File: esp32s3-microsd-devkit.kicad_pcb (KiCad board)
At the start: 4 copper layers, 53.1 x 49.5 mm, 28 parts, among them J1 Conn_01x17, J2 USB4105-GF-A, J3 Conn_01x17, U1 ESP32-S3-WROOM-1, U2 USBLC6-2P6, U3 MIC23150-SYMT-TR, X1 DM3AT-SF-PEJM5

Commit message: Ready to make v0.1
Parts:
- added D2: B0540WS-TP, Diode_SMD:D_SOD-123, F.Cu at (125.7, 91.0)
- added H1: MountingHole, MountingHole:MountingHole_2.2mm_M2_ISO7380_Pad, F.Cu at (121.0, 117.5)
- added H2: MountingHole, MountingHole:MountingHole_2.2mm_M2_ISO7380_Pad, F.Cu at (170.2, 69.2)
- added H3: MountingHole, MountingHole:MountingHole_2.2mm_M2_ISO7380_Pad, F.Cu at (170.2, 117.5)
- added TP1: TestPoint, TestPoint:TestPoint_Pad_1.5x1.5mm, F.Cu at (135.2, 107.9)
- added TP2: TestPoint, TestPoint:TestPoint_Pad_1.5x1.5mm, F.Cu at (127.7, 107.8)
- added TP3: TestPoint, TestPoint:TestPoint_Pad_1.5x1.5mm, F.Cu at (131.4, 107.8)
- moved J3 4.26 mm to (125.1, 117.5)
- moved J1 4.02 mm to (170.2, 73.0)
- renumbered BOOT1 to BOOT, RESET1 to RESET
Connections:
- J2 pad A4: +5V -> Net-(D2-A)
- J2 pad A9: +5V -> Net-(D2-A)
- J2 pad B4: +5V -> Net-(D2-A)
- J2 pad B9: +5V -> Net-(D2-A)
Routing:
- net Net-(D2-A): track 0.00 -> 41.6 mm, vias 0 -> 3
- net +3.3V: track 160.5 -> 170.2 mm
- net GPIO_35: track 17.4 -> 25.1 mm
- net +5V: track 90.1 -> 82.7 mm, vias 0 -> 3
- net GPIO_36: track 17.0 -> 23.7 mm
- net GPIO_39: track 14.6 -> 20.5 mm
- net GPIO_37: track 16.2 -> 22.1 mm
- net GPIO_45: track 19.9 -> 25.5 mm
- net GPIO_38: track 15.7 -> 21.1 mm
- net GPIO_40: track 13.7 -> 18.8 mm
- net GPIO_41: track 12.3 -> 17.1 mm
- net GPIO_21: track 29.5 -> 34.1 mm
- net GPIO_48: track 30.6 -> 35.2 mm
- net GPIO_47: track 30.0 -> 34.6 mm
- net GPIO_14: track 29.0 -> 33.6 mm
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- added copper zone on In2.Cu, net +3.3V
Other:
- board size 53.1 x 49.5 mm -> 54.4 x 53.3 mm
- board text added: "1"
- board text added: "10"
- board text added: "11"
- board text added: "12"
- board text added: "13"
- board text added: "14"
- board text added: "17"
- board text added: "18"
- board text added: "2"
- board text added: "21"
- board text added: "3"
- board text added: "3.3v"
- board text added: "35"
- board text added: "36"
- board text added: "37"
- board text added: "38"
- board text added: "39"
- board text added: "40"
- board text added: "41"
- board text added: "42"
- board text added: "45"
- board text added: "46"
- board text added: "47"
- board text added: "48"
- board text added: "5v"
- board text added: "8"
- board text added: "9"
- board text added: "ESP32S3 SD Devkit v0.1"
- board text added: "G"
- board text added: "GND"
- board text added: "RX"
- board text added: "Ride like a maniac into the light"
- board text added: "TX"

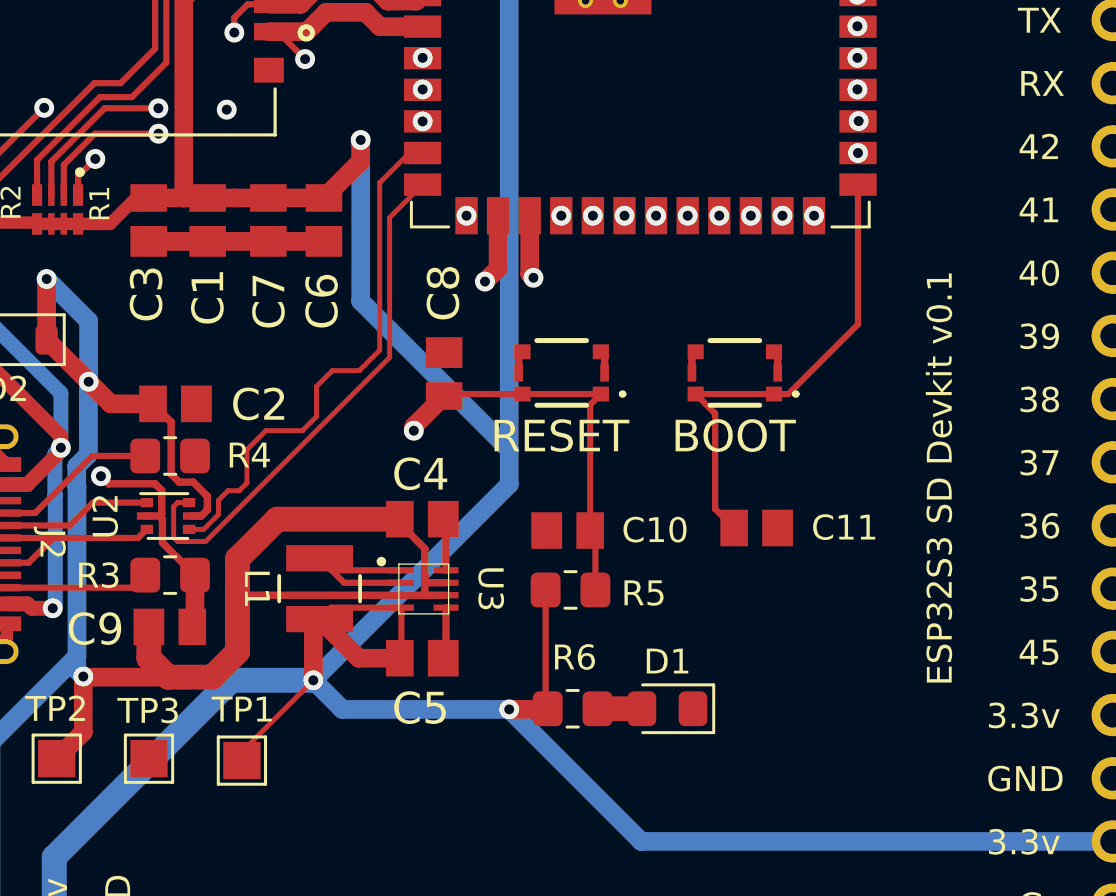
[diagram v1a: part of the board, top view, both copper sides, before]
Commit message: Fix cross-wired USB lines
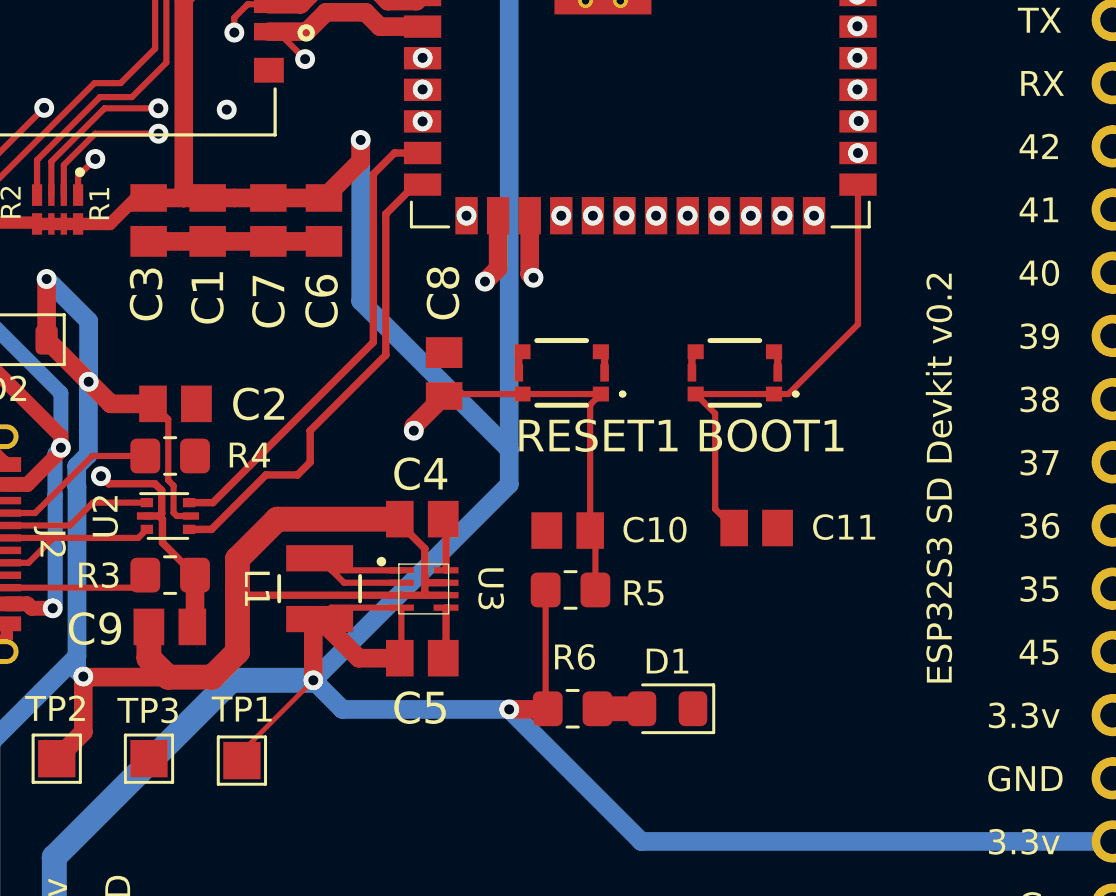
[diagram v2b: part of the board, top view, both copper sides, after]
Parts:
- added G***: LOGO, LOGO, B.Cu at (145.3, 91.8)
- renumbered BOOT to BOOT1, RESET to RESET1
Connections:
- U1 pad 13: /USB C/USB_D+ -> /USB C/USB_D-
- U1 pad 14: /USB C/USB_D- -> /USB C/USB_D+
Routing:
- net /USB C/USB_D+: track 21.4 -> 19.2 mm
- net /USB C/USB_D-: track 21.2 -> 19.2 mm
- net +5V: track 82.7 -> 82.0 mm
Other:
- board text added: "ESP32S3 SD Devkit v0.2"
- board text added: "Spidergod Industries"
- board text removed: "ESP32S3 SD Devkit v0.1"

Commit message: Update diode reference
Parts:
- D2: value B0540WS-TP -> MBR230LS
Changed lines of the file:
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@@
         (effects (font (size 1 1) (thickness 0.15)))
     )
-    (fp_text value "B0540WS-TP" (at 0 2.1) (layer "F.Fab") hide
+    (fp_text value "MBR230LS" (at 0 2.1) (layer "F.Fab") hide
         (effects (font (size 1 1) (thickness 0.15)))
     )
